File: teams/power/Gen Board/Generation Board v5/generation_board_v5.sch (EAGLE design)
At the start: 210 parts, among them U2 LT3652, U3 LT3652, U4 LT3652, U5 TPS732XX, U7 TPS732XX

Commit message: small changes to component values for distribution and generation board
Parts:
- R101, R102, R104, R105, R106, R107, R15, R16, R29, R32, R33, R34, R73, R74, R75, R77, R79, R80: value (none) -> DNP
- R103, R108, R112, R2, R30, R31, R76, R78, R84: value (none) -> 0
- R111, R37, R83: value (none) -> .1
- R17, R61, R89: value 520k -> 523k
- R19, R91: value .067 -> .09
- R20, R64, R92: value 545k -> 604k
- R21, R93: value 545k -> 143k
- R63: value .067 -> .11
- R65: value 545k -> 182k
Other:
- note added: "Center panel"
- note added: "I2C Address: 1000010"
- note added: "I2C Address: 1000011"
- note added: "I2C Address: 1000100"
- note added: "Imax=(2.409 [Vmpp] * 0.5029 [Impp] * 5 [# cells] * 80% [conversion efficiency] )/ 5.2 [Vbat_minimum] =0.932A Rshunt=0.11, giving 0.91A current limit"
- note added: "Imax=(2.409 [Vmpp] * 0.5029 [Impp] * 6 [# cells] * 80% [conversion efficiency] )/ 5.2 [Vbat_minimum] =1.118A Rshunt=0.09, giving 1.1A current limit"
- note added: "Vmpp=11.85V"
- note added: "Vmpp=14.22V"

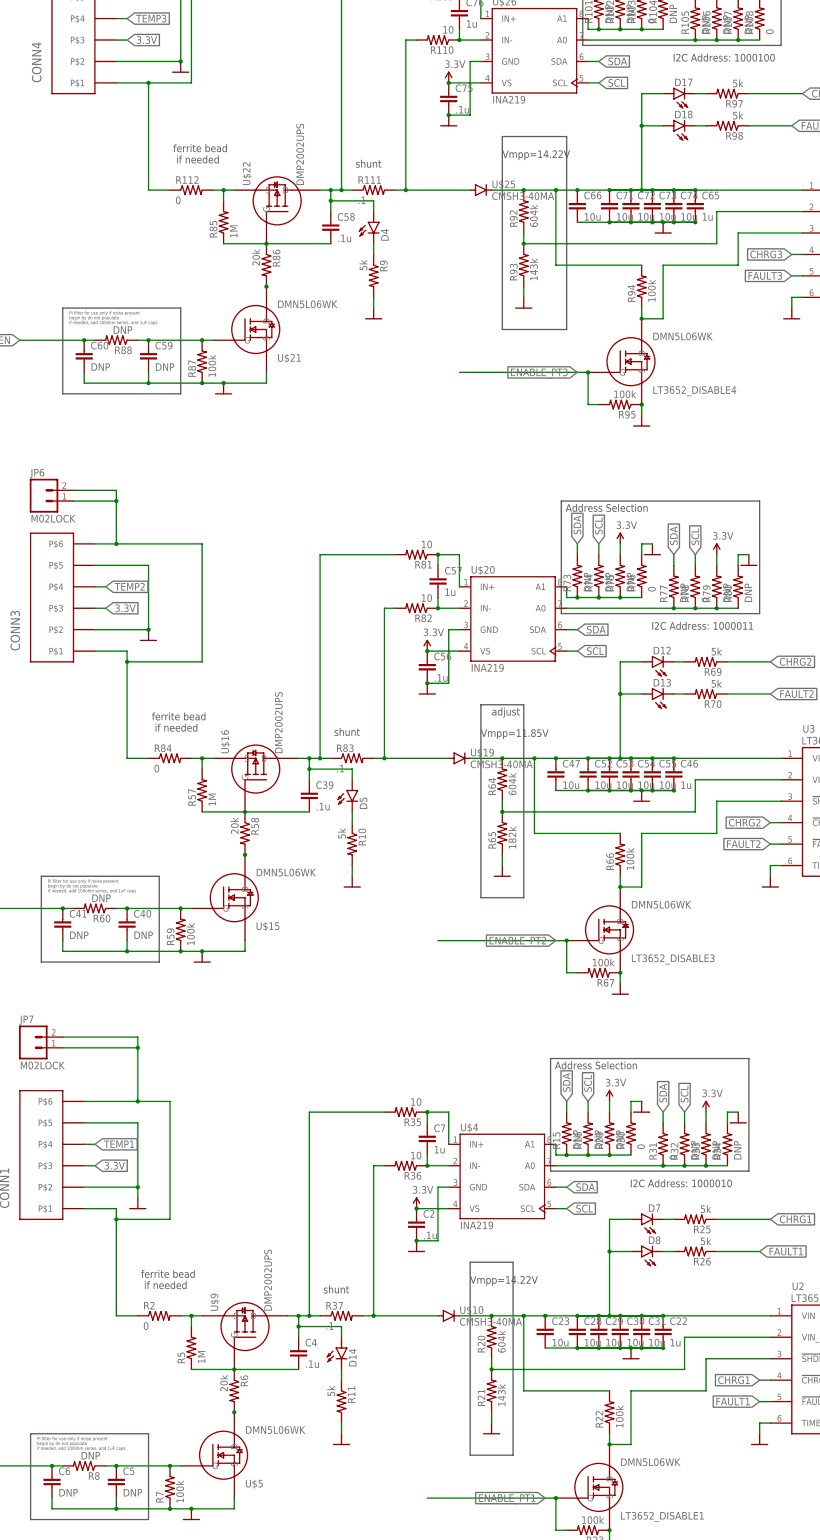
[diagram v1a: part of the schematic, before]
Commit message: fixed component values
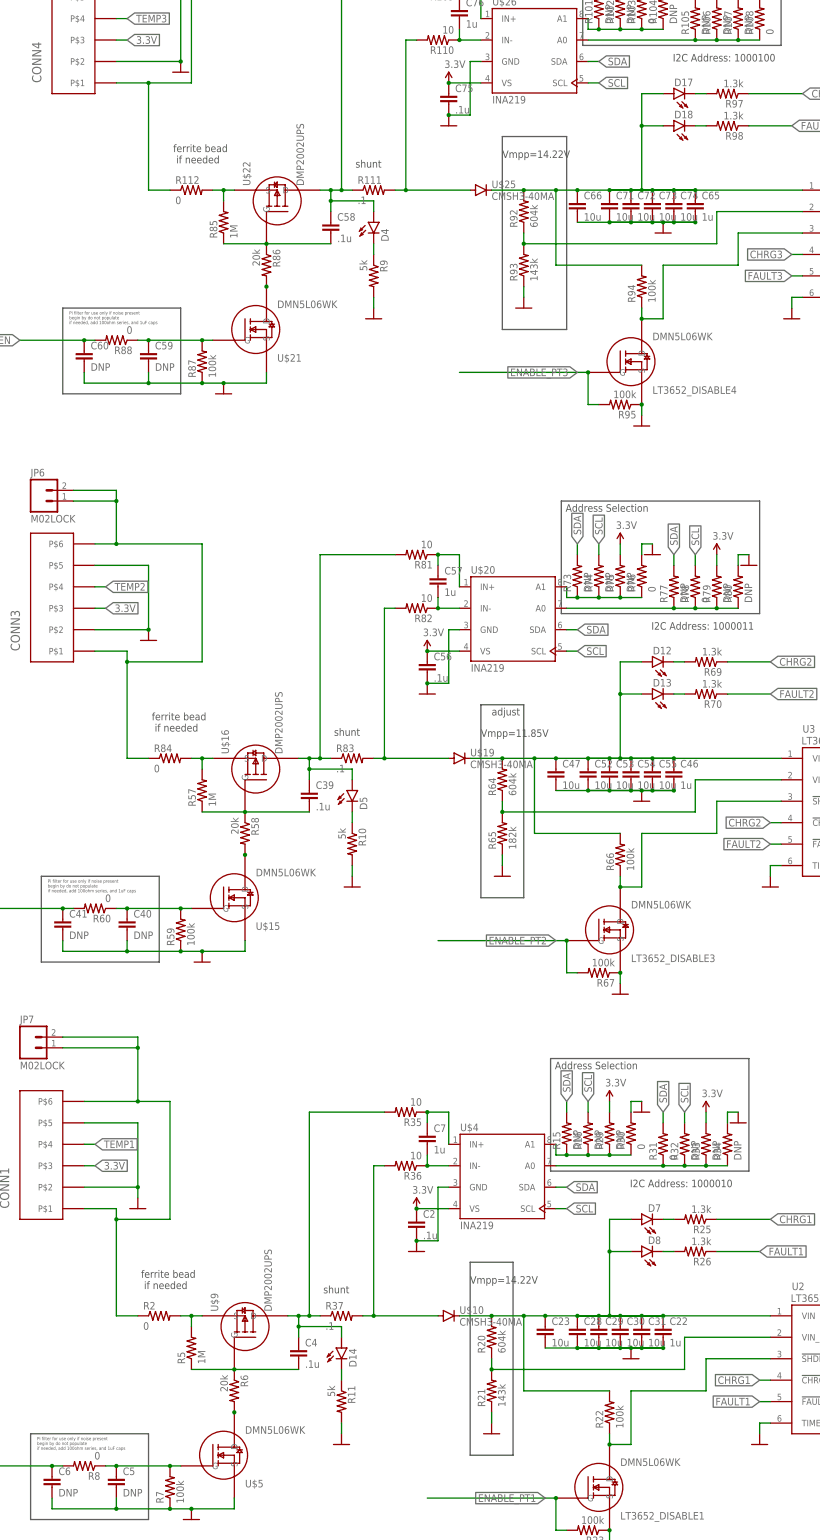
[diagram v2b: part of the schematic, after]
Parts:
- R25, R26, R69, R70, R97, R98: value 5k -> 1.3k
- R60, R8, R88: value DNP -> 0
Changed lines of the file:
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@@
 <part name="R7" library="DubSat1 Components" deviceset="RESISTOR" device="0805" value="100k"/>
 <part name="GND2" library="SparkFun-Aesthetics" deviceset="DGND" device=""/>
-<part name="R8" library="DubSat1 Components" deviceset="RESISTOR" device="0805" value="DNP"/>
+<part name="R8" library="DubSat1 Components" deviceset="RESISTOR" device="0805" value="0"/>
 <part name="C5" library="DubSat1 Components" deviceset="CAPACITOR" device="0805" value="DNP"/>
 <part name="C6" library="DubSat1 Components" deviceset="CAPACITOR" device="0805" value="DNP"/>
@@
 <part name="D7" library="DubSat1 Components" deviceset="LED" device=""/>
 <part name="D8" library="DubSat1 Components" deviceset="LED" device=""/>
-<part name="R25" library="DubSat1 Components" deviceset="RESISTOR" device="0805" value="5k"/>
-<part name="R26" library="DubSat1 Components" deviceset="RESISTOR" device="0805" value="5k"/>
+<part name="R25" library="DubSat1 Components" deviceset="RESISTOR" device="0805" value="1.3k"/>
+<part name="R26" library="DubSat1 Components" deviceset="RESISTOR" device="0805" value="1.3k"/>
 <part name="GND22" library="SparkFun-Aesthetics" deviceset="DGND" device=""/>
 <part name="C28" library="DubSat1 Components" deviceset="CAPACITOR" device="1210" value="10u"/>
@@
 <part name="R59" library="DubSat1 Components" deviceset="RESISTOR" device="0805" value="100k"/>
 <part name="GND35" library="SparkFun-Aesthetics" deviceset="DGND" device=""/>
-<part name="R60" library="DubSat1 Components" deviceset="RESISTOR" device="0805" value="DNP"/>
+<part name="R60" library="DubSat1 Components" deviceset="RESISTOR" device="0805" value="0"/>
 <part name="C40" library="DubSat1 Components" deviceset="CAPACITOR" device="0805" value="DNP"/>
 <part name="C41" library="DubSat1 Components" deviceset="CAPACITOR" device="0805" value="DNP"/>
@@
 <part name="D12" library="DubSat1 Components" deviceset="LED" device=""/>
 <part name="D13" library="DubSat1 Components" deviceset="LED" device=""/>
-<part name="R69" library="DubSat1 Components" deviceset="RESISTOR" device="0805" value="5k"/>
-<part name="R70" library="DubSat1 Components" deviceset="RESISTOR" device="0805" value="5k"/>
+<part name="R69" library="DubSat1 Components" deviceset="RESISTOR" device="0805" value="1.3k"/>
+<part name="R70" library="DubSat1 Components" deviceset="RESISTOR" device="0805" value="1.3k"/>
 <part name="GND45" library="SparkFun-Aesthetics" deviceset="DGND" device=""/>
 <part name="C52" library="DubSat1 Components" deviceset="CAPACITOR" device="1210" value="10u"/>
@@
 <part name="R87" library="DubSat1 Components" deviceset="RESISTOR" device="0805" value="100k"/>
 <part name="GND52" library="SparkFun-Aesthetics" deviceset="DGND" device=""/>
-<part name="R88" library="DubSat1 Components" deviceset="RESISTOR" device="0805" value="DNP"/>
+<part name="R88" library="DubSat1 Components" deviceset="RESISTOR" device="0805" value="0"/>
 <part name="C59" library="DubSat1 Components" deviceset="CAPACITOR" device="0805" value="DNP"/>
 <part name="C60" library="DubSat1 Components" deviceset="CAPACITOR" device="0805" value="DNP"/>
@@
 <part name="D17" library="DubSat1 Components" deviceset="LED" device=""/>
 <part name="D18" library="DubSat1 Components" deviceset="LED" device=""/>
-<part name="R97" library="DubSat1 Components" deviceset="RESISTOR" device="0805" value="5k"/>
-<part name="R98" library="DubSat1 Components" deviceset="RESISTOR" device="0805" value="5k"/>
+<part name="R97" library="DubSat1 Components" deviceset="RESISTOR" device="0805" value="1.3k"/>
+<part name="R98" library="DubSat1 Components" deviceset="RESISTOR" device="0805" value="1.3k"/>
 <part name="GND62" library="SparkFun-Aesthetics" deviceset="DGND" device=""/>
 <part name="C71" library="DubSat1 Components" deviceset="CAPACITOR" device="1210" value="10u"/>

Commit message: minor changes
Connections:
- net ENABLE_PT1 renamed DISABLE_PT1
- new net DISABLE_PT2: BLK1.P3.6_GPIO/PWM
- new net DISABLE_PT3: BLK1.P2.6_GPIO/PWM
- net ENABLE_PT2: no longer BLK1.P3.6_GPIO/PWM
- net ENABLE_PT3: no longer BLK1.P2.6_GPIO/PWM
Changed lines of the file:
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@@
 </segment>
 </net>
-<net name="ENABLE_PT1" class="0">
+<net name="DISABLE_PT1" class="0">
 <segment>
 <pinref part="R23" gate="G$1" pin="2"/>
@@
 <junction x="185.42" y="223.52"/>
 </segment>
-<segment>
-<pinref part="BLK1" gate="G$1" pin="P3.6_GPIO/PWM"/>
-<wire x1="-86.36" y1="289.56" x2="-83.82" y2="289.56" width="0.1524" layer="91"/>
-<label x="-83.82" y="289.56" size="1.778" layer="95" xref="yes"/>
-</segment>
 </net>
 <net name="N$23" class="0">
@@
 <junction x="190.5" y="358.14"/>
 </segment>
-<segment>
-<pinref part="BLK1" gate="G$1" pin="P2.6_GPIO/PWM"/>
-<wire x1="-86.36" y1="284.48" x2="-83.82" y2="284.48" width="0.1524" layer="91"/>
-<label x="-83.82" y="284.48" size="1.778" layer="95" xref="yes"/>
-</segment>
 </net>
 <net name="N$32" class="0">
@@
 </segment>
 </net>
+<net name="DISABLE_PT2" class="0">
+<segment>
+<pinref part="BLK1" gate="G$1" pin="P3.6_GPIO/PWM"/>
+<wire x1="-86.36" y1="289.56" x2="-83.82" y2="289.56" width="0.1524" layer="91"/>
+<label x="-83.82" y="289.56" size="1.778" layer="95" xref="yes"/>
+</segment>
+</net>
+<net name="DISABLE_PT3" class="0">
+<segment>
+<pinref part="BLK1" gate="G$1" pin="P2.6_GPIO/PWM"/>
+<wire x1="-86.36" y1="284.48" x2="-83.82" y2="284.48" width="0.1524" layer="91"/>
+<label x="-83.82" y="284.48" size="1.778" layer="95" xref="yes"/>
+</segment>
+</net>
